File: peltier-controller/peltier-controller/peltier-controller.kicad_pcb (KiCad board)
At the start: 2 copper layers, 43.2 x 29.1 mm, 18 parts, among them J1 Peltier_Terminal, J2 Conn_01x03_Pin, J3 PWR_IN_15V, K1 SANYOU_SRD_Form_C, Q1 MJE3055, U1 ATtiny84A-SS, U2 AMS1117-3.3

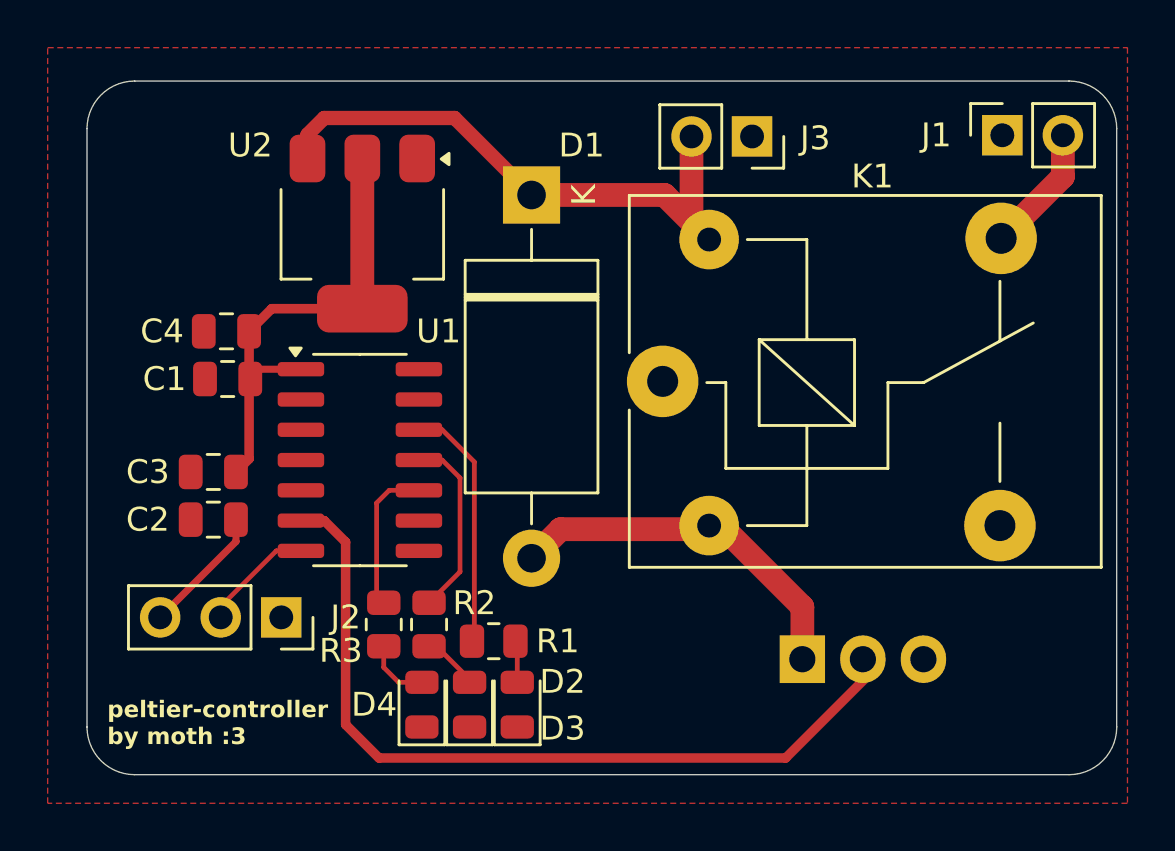
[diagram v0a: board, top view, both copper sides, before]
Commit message: updated peltier
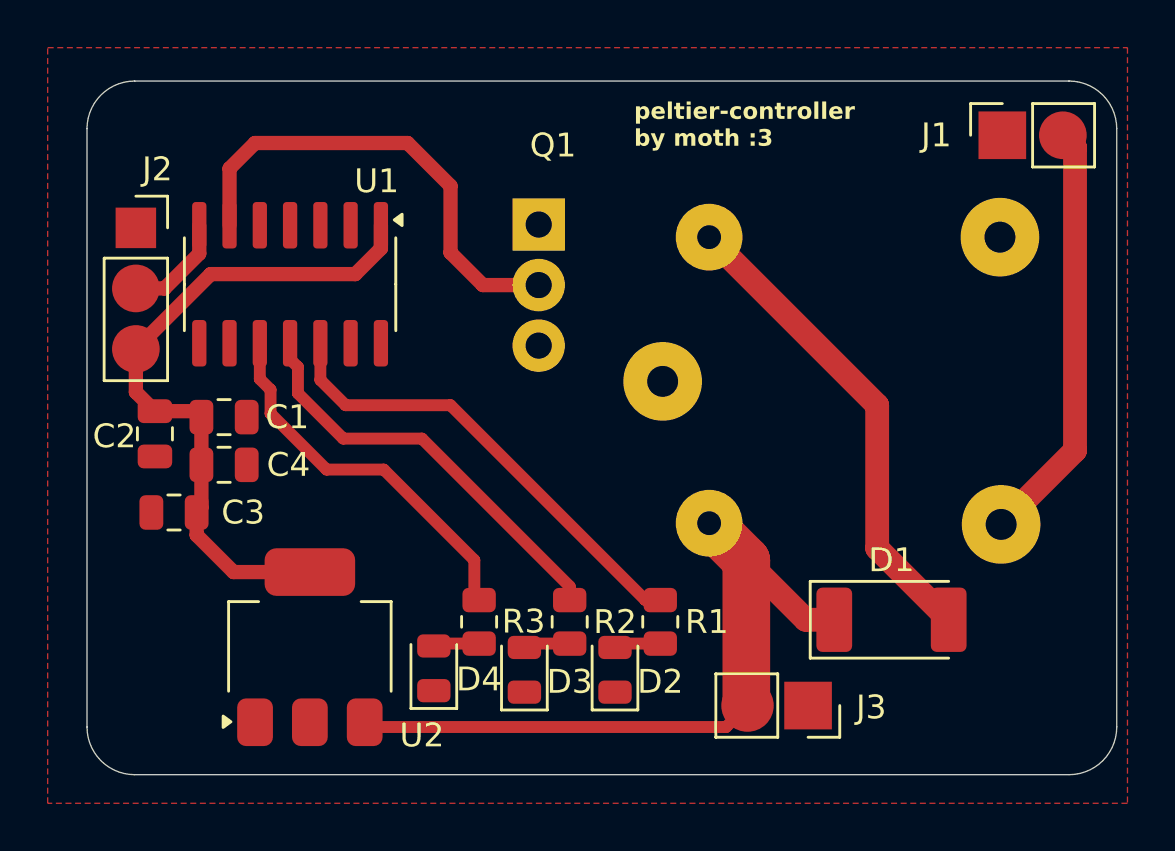
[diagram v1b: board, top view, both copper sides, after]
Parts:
- D1: footprint Diode_THT:D_DO-27_P15.24mm_Horizontal -> Diode_SMD:D_MELF
- K1: moved to B.Cu
- moved J3 24.0 mm to (105.2, 68.6)
- moved D1 23.4 mm to (108.7, 65.0), turned to 0 degrees
- moved Q1 21.3 mm to (93.9, 48.4), turned to -90 degrees
- moved U2 17.5 mm to (84.3, 66.2), turned to 90 degrees
- moved J2 17.4 mm to (77.0, 48.6), turned to 0 degrees
- moved U1 7.94 mm to (83.5, 50.9), turned to -90 degrees
- moved R1 7.03 mm to (99.0, 65.1), turned to 90 degrees
- moved R2 5.90 mm to (95.2, 65.1)
- moved C4 5.60 mm to (80.7, 58.5), turned to 0 degrees
- moved C2 4.35 mm to (77.8, 57.2), turned to -90 degrees
- moved D2 4.35 mm to (97.1, 67.1)
- moved R3 4.00 mm to (91.4, 65.1)
- moved D3 2.73 mm to (93.3, 67.1)
- moved C3 2.37 mm to (78.6, 60.5)
- moved C1 1.61 mm to (80.7, 56.5), turned to 0 degrees
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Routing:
- net RELAY_CTRL: track 33.6 -> 19.9 mm
- net 15V_NC: track 5.40 -> 17.8 mm
- net PA2_TEMP_LED: track 7.81 -> 17.6 mm
- net PA3_HEATER_LED: track 6.31 -> 16.0 mm
- net PA1_PWR_LED: track 10.8 -> 19.6 mm
- net VCC: track 24.9 -> 31.8 mm
- net Net-(D1-A): track 15.5 -> 21.1 mm
- net +5V: track 25.3 -> 28.4 mm
- net Net-(D4-A): track 2.75 -> 1.94 mm

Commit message: add updated files
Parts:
- moved C3 3.10 mm to (79.7, 63.4), turned to -90 degrees
- moved C2 2.16 mm to (78.0, 59.4)
- moved C1 2.10 mm to (80.7, 58.6)
- moved C4 2.10 mm to (80.7, 60.6)
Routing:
- net Net-(D1-A): track 21.1 -> 28.8 mm
- net +5V: track 28.4 -> 35.0 mm
- net RELAY_CTRL: track 19.9 -> 16.3 mm
- net PA3_HEATER_LED: track 16.0 -> 14.7 mm
- net PA2_TEMP_LED: track 17.6 -> 17.0 mm
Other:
- outline, holes or cut-outs redrawn
